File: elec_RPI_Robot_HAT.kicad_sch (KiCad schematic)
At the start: 6 parts

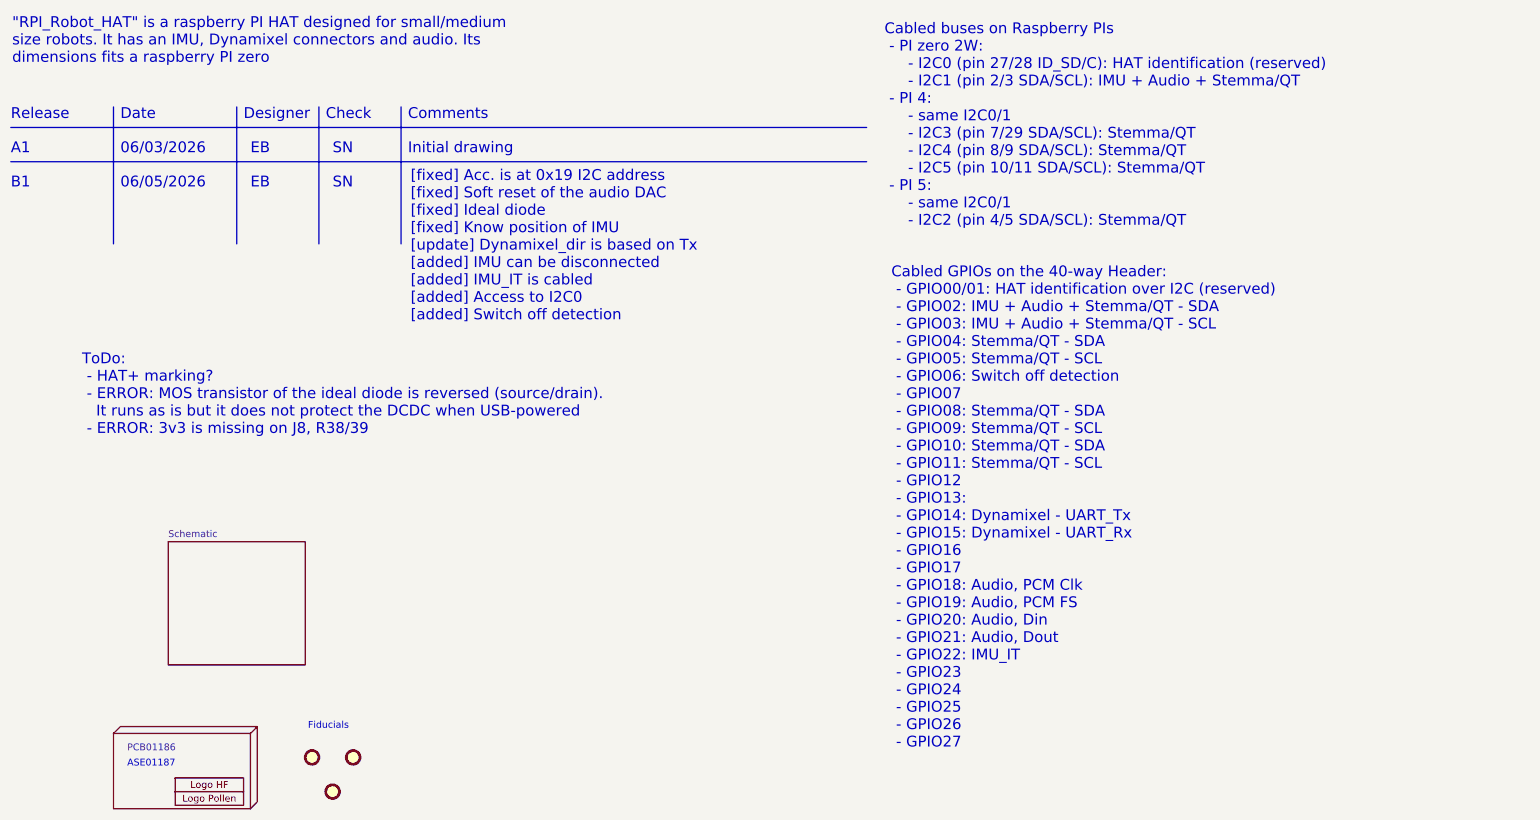
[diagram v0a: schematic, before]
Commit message: [update] Release C1 (for Grabette), now qtty 20 @JLCPCB
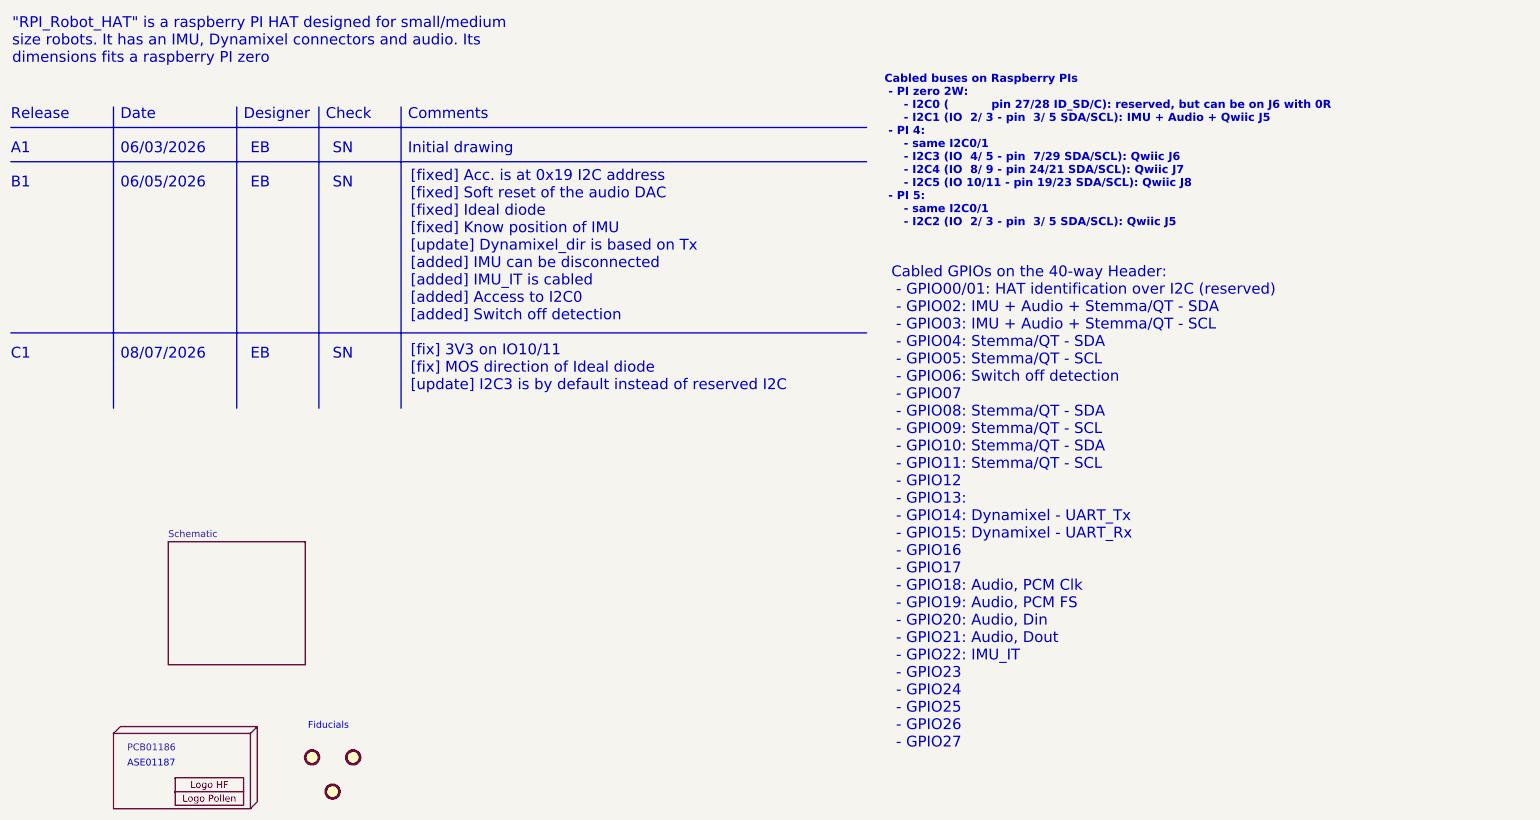
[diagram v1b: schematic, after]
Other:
- note added: "08/07/2026"
- note added: "C1"
- note added: "Cabled buses on Raspberry PIs - PI zero 2W: - I2C0 ( pin 27/28 ID_SD/C): reserved, but can be on J6 with 0R - I2C1 (IO 2/ 3 - pin 3/ 5 SDA/SCL): IMU + Audio + Qwiic J5 - PI 4: - same I2C0/1 - I2C3 (IO 4/ 5 - pin 7/29 SDA/SCL): Qwiic J6 - I2C4 (IO 8/ 9 - pin 24/21 SDA/SCL): Qwiic J7 - I2C5 (IO 10/11 - pin 19/23 SDA/SCL): Qwiic J8 - PI 5: - same I2C0/1 - I2C2 (IO 2/ 3 - pin 3/ 5 SDA/SCL): Qwiic J5"
- note added: "[fix] 3V3 on IO10/11 [fix] MOS direction of Ideal diode [update] I2C3 is by default instead of reserved I2C"
- note removed: "Cabled buses on Raspberry PIs - PI zero 2W: - I2C0 (pin 27/28 ID_SD/C): HAT identification (reserved) - I2C1 (pin 2/3 SDA/SCL): IMU + Audio + Stemma/QT - PI 4: - same I2C0/1 - I2C3 (pin 7/29 SDA/SCL): Stemma/QT - I2C4 (pin 8/9 SDA/SCL): Stemma/QT - I2C5 (pin 10/11 SDA/SCL): Stemma/QT - PI 5: - same I2C0/1 - I2C2 (pin 4/5 SDA/SCL): Stemma/QT"
- note removed: "ToDo: - HAT+ marking? - ERROR: MOS transistor of the ideal diode is reversed (source/drain). It runs as is but it does not protect the DCDC when USB-powered - ERROR: 3v3 is missing on J8, R38/39"
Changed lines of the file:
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@@
+		)
+	)
+	(text "C1"
+		(exclude_from_sim no)
+		(at 19.05 82.55 0)
+		(effects
+			(font
+				(size 2.0066 2.0066)
+			)
+			(justify left bottom)
+		)
+	)
+	(text "[fix] 3V3 on IO10/11\n[fix] MOS direction of Ideal diode\n[update] I2C3 is by default instead of reserved I2C"
+		(exclude_from_sim no)
+		(at 93.218 88.392 0)
+		(effects
+			(font
+				(size 2.0066 2.0066)
+			)
+			(justify left bottom)
 		)
 	)
@@
 		)
 	)
+	(text "EB"
+		(exclude_from_sim no)
+		(at 63.5 82.55 0)
+		(effects
+			(font
+				(size 2.0066 2.0066)
+			)
+			(justify left bottom)
+		)
+	)
 	(text "Release"
 		(exclude_from_sim no)
@@
 		)
 	)
-	(text "Cabled buses on Raspberry PIs\n - PI zero 2W:\n     - I2C0 (pin 27/28 ID_SD/C): HAT identification (reserved)\n     - I2C1 (pin 2/3 SDA/SCL): IMU + Audio + Stemma/QT\n - PI 4:\n     - same I2C0/1\n     - I2C3 (pin 7/29 SDA/SCL): Stemma/QT\n     - I2C4 (pin 8/9 SDA/SCL): Stemma/QT\n     - I2C5 (pin 10/11 SDA/SCL): Stemma/QT\n - PI 5:\n     - same I2C0/1\n     - I2C2 (pin 4/5 SDA/SCL): Stemma/QT"
+	(text "Cabled buses on Raspberry PIs\n - PI zero 2W:\n     - I2C0 (           pin 27/28 ID_SD/C): reserved, but can be on J6 with 0R\n     - I2C1 (IO  2/ 3 - pin  3/ 5 SDA/SCL): IMU + Audio + Qwiic J5\n - PI 4:\n     - same I2C0/1\n     - I2C3 (IO  4/ 5 - pin  7/29 SDA/SCL): Qwiic J6\n     - I2C4 (IO  8/ 9 - pin 24/21 SDA/SCL): Qwiic J7\n     - I2C5 (IO 10/11 - pin 19/23 SDA/SCL): Qwiic J8\n - PI 5:\n     - same I2C0/1\n     - I2C2 (IO  2/ 3 - pin  3/ 5 SDA/SCL): Qwiic J5"
 		(exclude_from_sim no)
 		(at 181.102 57.912 0)
 		(effects
 			(font
-				(size 2.0066 2.0066)
-			)
-			(justify left bottom)
-		)
-	)
-	(text "ToDo:\n - HAT+ marking?\n - ERROR: MOS transistor of the ideal diode is reversed (source/drain). \n   It runs as is but it does not protect the DCDC when USB-powered\n - ERROR: 3v3 is missing on J8, R38/39"
-		(exclude_from_sim no)
-		(at 32.258 96.52 0)
+				(face "Liberation Mono")
+				(size 1.5 1.5)
+				(bold yes)
+			)
+			(justify left bottom)
+		)
+	)
+	(text "08/07/2026"
+		(exclude_from_sim no)
+		(at 39.37 82.55 0)
 		(effects
 			(font
@@
 		)
 	)
+	(text "SN"
+		(exclude_from_sim no)
+		(at 78.74 82.55 0)
+		(effects
+			(font
+				(size 2.0066 2.0066)
+			)
+			(justify left bottom)
+		)
+	)
 	(text "B1"
 		(exclude_from_sim no)
@@
 	(polyline
 		(pts
-			(xy 91.44 35.56) (xy 91.44 60.96)
-		)
-		(stroke
-			(width 0)
-			(type default)
-		)
-	)
-	(polyline
-		(pts
-			(xy 38.1 35.56) (xy 38.1 60.96)
+			(xy 91.44 35.56) (xy 91.44 91.44)
+		)
+		(stroke
+			(width 0)
+			(type default)
+		)
+	)
+	(polyline
+		(pts
+			(xy 38.1 35.56) (xy 38.1 91.44)
 		)
 		(stroke
@@
 	(polyline
 		(pts
-			(xy 60.96 35.56) (xy 60.96 60.96)
-		)
-		(stroke
-			(width 0)
-			(type default)
-		)
-	)
-	(polyline
-		(pts
-			(xy 76.2 35.56) (xy 76.2 60.96)
-		)
-		(stroke
+			(xy 19.05 77.47) (xy 177.8 77.47)
+		)
+		(stroke
+			(width 0)
+			(type default)
+		)
+	)
+	(polyline
+		(pts
+			(xy 60.96 35.56) (xy 60.96 91.44)
+		)
+		(stroke
+			(width 0)
+			(type default)
+		)
+	)
+	(polyline
+		(pts
+			(xy 76.2 35.56) (xy 76.2 91.44)
+		)
+		(stroke
